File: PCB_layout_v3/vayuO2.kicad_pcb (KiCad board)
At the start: 2 copper layers, 124 x 88 mm, 165 parts, among them CN1 Conn_LED, CN10 OUT, CN11 OUT, CN12 OUT, CN13 OUT, CN14 Conn_Analog, CN15 Conn_ADS1115, CN16 Conn_S1, CN17 Conn_S2, CN18 Conn_S3, CN19 Conn_O2_5V, CN2 UART1, CN3 UART2, CN4 I2C_1, CN5 I2C_2, CN7 24VDC, CN9 OUT, J1 DS3231_BO, J10 Conn_01x01, J11 Conn_01x01, J12 Conn_01x01, J13 Conn_01x01, J14 Conn_01x01, J15 Conn_01x01, J2 Conn_01x01, J3 Conn_01x01, J4 Conn_01x01, J5 Conn_01x01, J6 Conn_01x01, J7 Conn_01x01, J8 Conn_01x01, J9 Conn_01x01, Q1 MMBT3904, Q10 BSS138, Q11 BSS138, Q12 BSS138, Q3 IRF540NS, Q4 IRF540NS, Q5 IRF540NS, Q6 IRF540NS, Q7 IRF540NS, Q8 BSS138, Q9 BSS138, U1 ESP32_breakout, U10 PS2801-1, U11 DC_DC_buck_6W, U12 PS2801-1, U2 DS3231SN#T&R, U3 B2405S-2WR2, U4 LM1117-33, U6 24V_BUCK, U7 PS2801-1, U8 PS2801-1, U9 PS2801-1

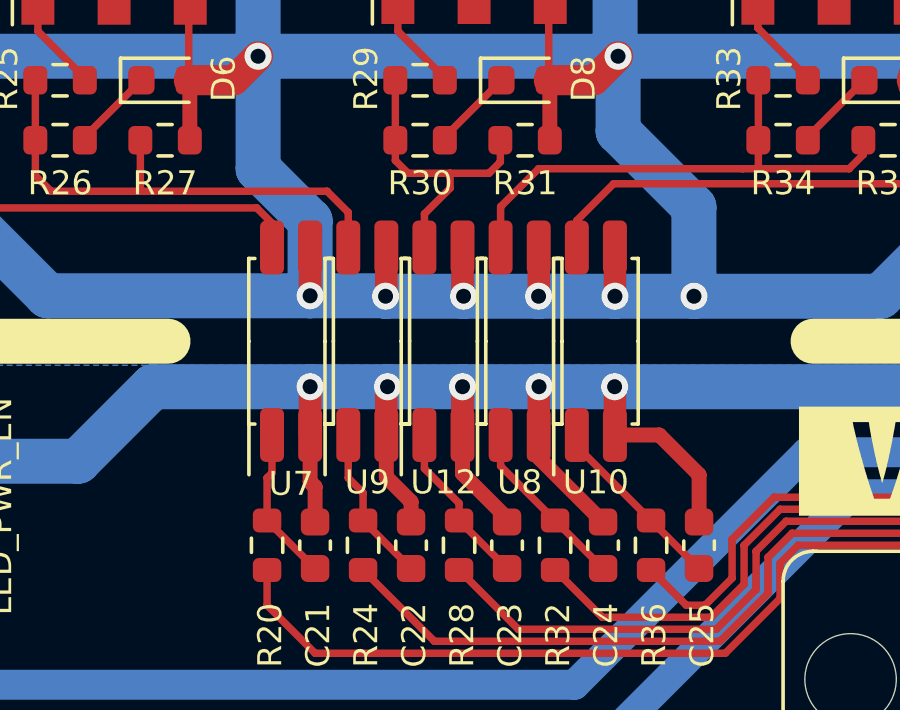
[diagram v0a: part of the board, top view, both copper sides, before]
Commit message: Updated component footprint
* Updated opto IC footprint

Co-Authored-By: Anool Mahidharia <anool.m@gmail.com>
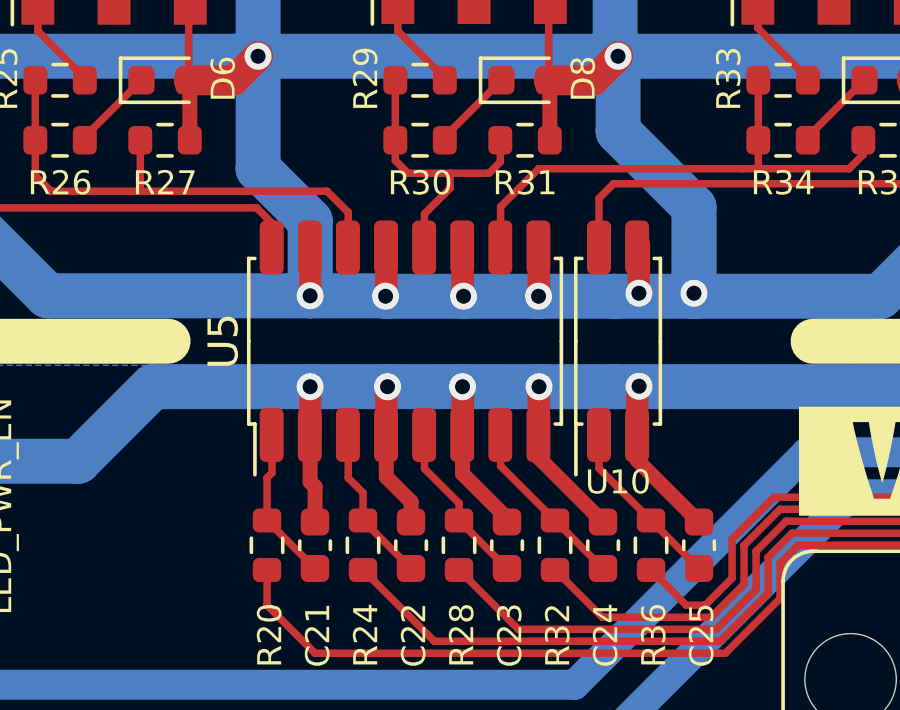
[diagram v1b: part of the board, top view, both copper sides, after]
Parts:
- removed U12, U7, U8, U9: PS2801-1, AA_vayu:SO-4_5.3x2.7mm_P1.27mm
- added U5: PS2801-4, AA_vayu:SO-16_5.3x10.2mm_P1.27mm, F.Cu at (98.9, 89.5)
- moved U10 0.74 mm to (106.0, 89.5)
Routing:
- net GND: track 681.0 -> 679.8 mm

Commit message: ver 3 production files ready
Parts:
- added kibuzzard-61681EBC: G***, label, F.Cu at (123.1, 136.4)
- moved G2 5.55 mm to (148.3, 134.4)
- moved G3 5.30 mm to (158.0, 134.2)
- moved G1 3.73 mm to (154.0, 109.5)
- moved kibuzzard-615EFBF6 1.78 mm to (151.6, 121.7)
